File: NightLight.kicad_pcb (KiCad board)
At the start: 2 copper layers, 88 x 88 mm, 17 parts, among them U1 magnetic-charger, U2 rdm-6300, U3 TP4056, U4 ESP32-WROOM-32

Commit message: Add lots of ocmponents
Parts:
- added C1: 22u, Capacitor_THT:CP_Radial_D5.0mm_P2.50mm, F.Cu at (101.0, 116.2)
- added J1: Conn_01x02, Connector_PinHeader_2.54mm:PinHeader_1x02_P2.54mm_Vertical, F.Cu at (95.5, 93.5)
- added J2: Micro_SD_Card, sd-card:sd-card, F.Cu at (99.5, 121.2)
- added U5: AMS1117-3.3, Package_TO_SOT_SMD:SOT-223-3_TabPin2, B.Cu at (97.3, 111.3)
- D7, U1: moved to B.Cu
- moved U3 46.0 mm to (142.6, 109.8), turned to 180 degrees
- moved BT1 16.8 mm to (111.5, 108.8), turned to 180 degrees
- moved R1 16.7 mm to (89.5, 69.0), turned to 0 degrees
- moved D7 5.00 mm to (93.0, 65.0), turned to 180 degrees
- moved U4 5.00 mm to (73.0, 100.0)
- moved R2 2.25 mm to (111.2, 105.5)
- moved R3 2.25 mm to (111.2, 98.5)
- turned U1 to 180 degrees
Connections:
- U2 pad 6: unconnected-(U2-Pad6) -> Net-(J1-Pad1)
- U2 pad 7: unconnected-(U2-Pad7) -> Net-(J1-Pad2)
- U3 pad 3: +3V3 -> +4V
- U4 pad 10: unconnected-(U4-Pad10) -> DAC1
- U4 pad 11: unconnected-(U4-Pad11) -> DAC2
- U4 pad 12: unconnected-(U4-Pad12) -> TOUCH3
- U4 pad 8: unconnected-(U4-Pad8) -> TOUCH1
- U4 pad 9: unconnected-(U4-Pad9) -> TOUCH2
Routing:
- net Net-(D5-Pad1): track 70.8 -> 0.00 mm
- net unconnected-(U2-Pad4): track 42.7 -> 0.00 mm
- net PHOTO_VOLTAGE: track 38.8 -> 0.00 mm
- net GND: track 36.3 -> 0.00 mm
- net +5V: track 35.9 -> 0.00 mm
- net +3V3: track 35.1 -> 0.00 mm
- net Net-(D2-Pad1): track 35.0 -> 0.00 mm
- net +BATT: track 24.6 -> 0.00 mm
- net -BATT: track 13.1 -> 0.00 mm
- net ADC_BAT: track 1.92 -> 0.00 mm
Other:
- outline, holes or cut-outs redrawn
- board text added: "TODO: - Batterie ausmessen - Speaker Optionen auschecken - How far does the SD card protrude"

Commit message: Add button and update the magnetic charger
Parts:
- added R4: 10k, Resistor_THT:R_Axial_DIN0204_L3.6mm_D1.6mm_P5.08mm_Horizontal, F.Cu at (61.5, 82.8)
- added SW1: POWER-ON, Button_Switch_SMD:SW_SPDT_CK-JS102011SAQN, B.Cu at (128.6, 129.4)
- U5: footprint Package_TO_SOT_SMD:SOT-223-3_TabPin2 -> Package_TO_SOT_SMD:TO-252-2
- moved U5 4.15 mm to (93.3, 110.5)
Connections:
- U2 pad 4: unconnected-(U2-Pad4) -> RFID_TX
- U5 pad 3: +4V -> /+4V_Switched

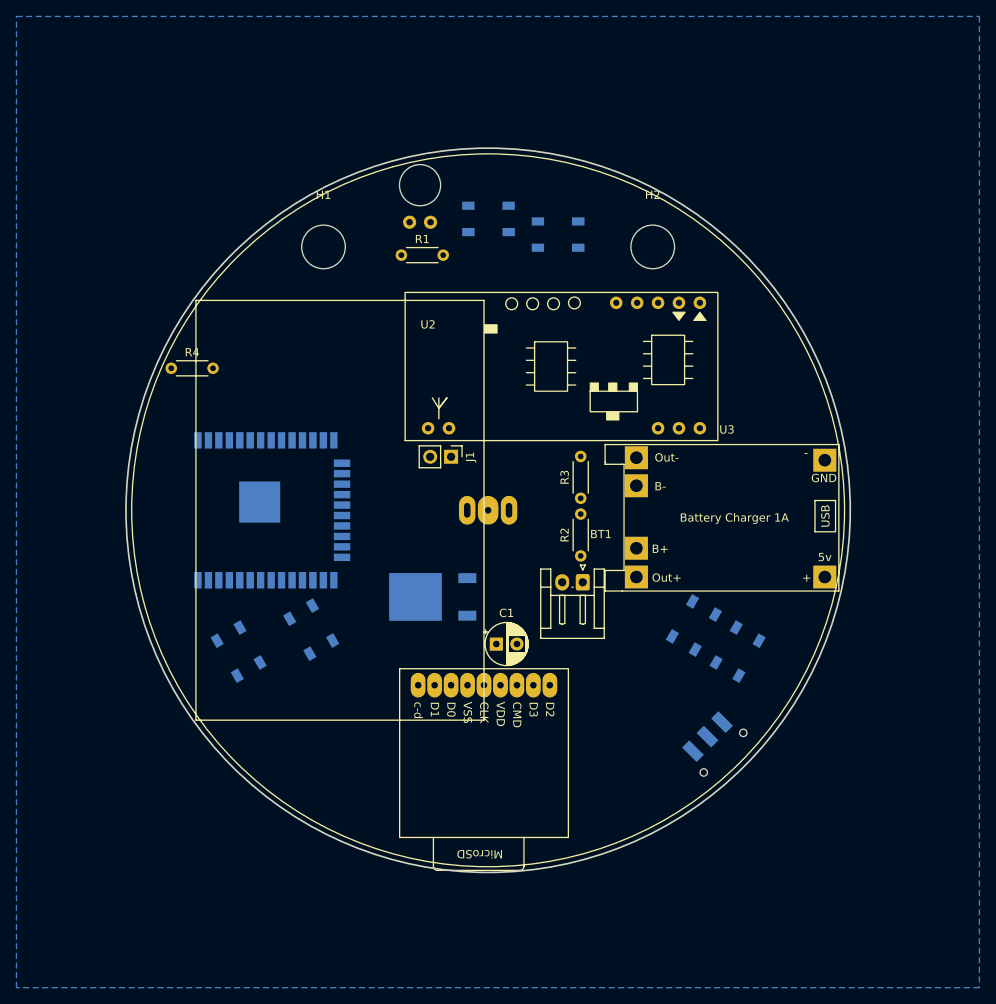
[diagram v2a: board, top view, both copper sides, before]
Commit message: Updates from card board prototype
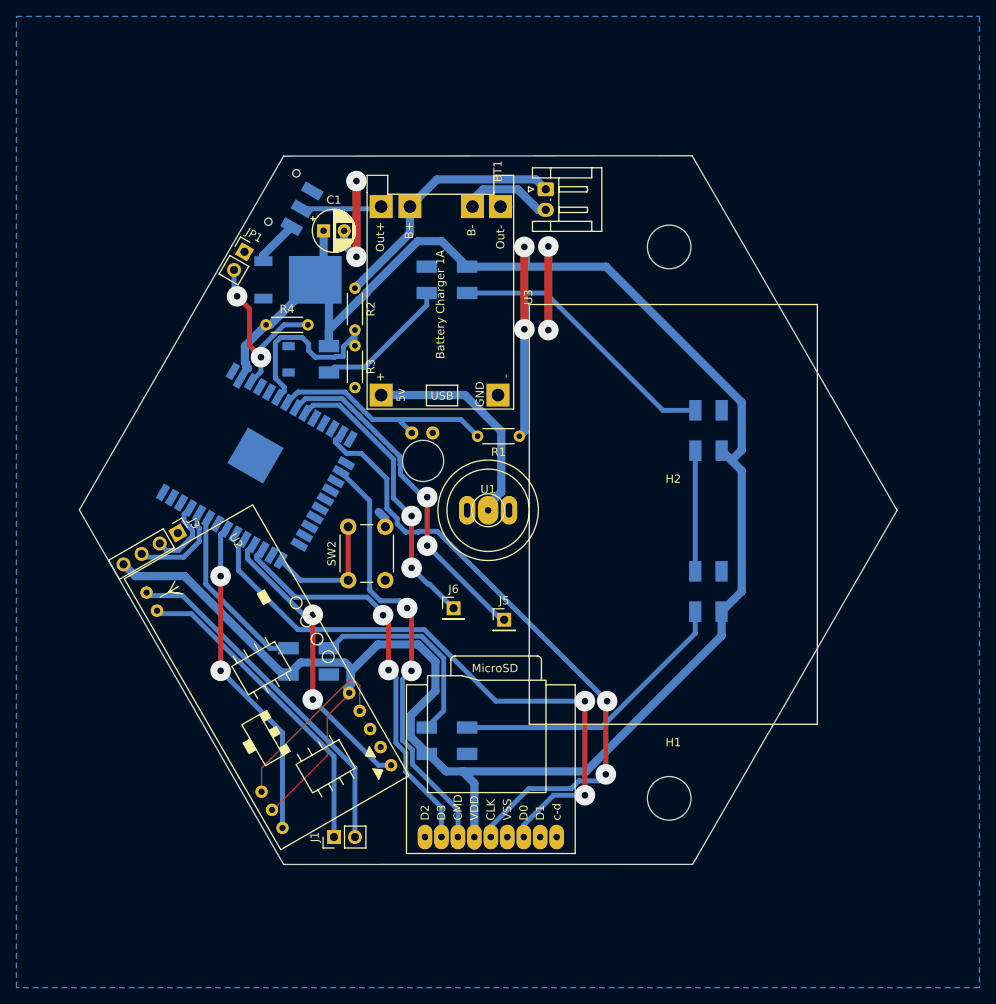
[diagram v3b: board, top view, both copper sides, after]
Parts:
- added J3: TTL, Connector_PinHeader_2.54mm:PinHeader_1x04_P2.54mm_Vertical, F.Cu at (62.3, 102.8)
- added J5: Touch1, Connector_PinHeader_2.54mm:PinHeader_1x01_P2.54mm_Vertical, F.Cu at (102.0, 113.3)
- added J6: Touch2, Connector_PinHeader_2.54mm:PinHeader_1x01_P2.54mm_Vertical, F.Cu at (95.8, 111.9)
- added JP1: Jumper_2_Open, Connector_PinHeader_2.54mm:PinHeader_1x02_P2.54mm_Vertical, F.Cu at (70.4, 68.6)
- added SW2: SW_Push, Button_Switch_THT:SW_PUSH_6mm_H4.3mm, F.Cu at (83.0, 108.5)
- U1: moved to F.Cu
- moved SW1 86.2 mm to (75.0, 62.0), turned to 60 degrees
- moved H1 78.9 mm to (122.5, 134.5)
- moved U2 63.5 mm to (79.0, 130.4), turned to -60 degrees
- moved U3 61.4 mm to (85.3, 87.7), turned to 90 degrees
- moved D1 60.1 mm to (78.2, 118.4), turned to 180 degrees
- moved C1 54.4 mm to (80.0, 66.0)
- moved D4 54.0 mm to (126.8, 90.3), turned to -90 degrees
- moved D5 51.8 mm to (95.0, 72.0), turned to 0 degrees
- moved J1 48.3 mm to (81.3, 139.7), turned to 90 degrees
- moved BT1 48.0 mm to (107.0, 61.0), turned to -90 degrees
- moved R2 42.6 mm to (83.8, 73.0), turned to -90 degrees
- moved U5 41.9 mm to (76.9, 72.0), turned to 0 degrees
- moved H2 34.6 mm to (122.5, 102.5)
- moved D2 33.1 mm to (95.0, 128.0), turned to 180 degrees
- moved R3 33.1 mm to (83.8, 80.0), turned to -90 degrees
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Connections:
- U4 pad 12: TOUCH3 -> unconnected-(U4-Pad12)
- U4 pad 28: unconnected-(U4-Pad28) -> RFID_TX
- U4 pad 31: unconnected-(U4-Pad31) -> RFID_LED
- U4 pad 33: unconnected-(U4-Pad33) -> Neopixel
- U4 pad 6: unconnected-(U4-Pad6) -> ADC_BAT
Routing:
- net +3V3: track 0.00 -> 288.6 mm, vias 0 -> 2
- net SCK: track 0.00 -> 77.8 mm, vias 0 -> 2
- net MISO: track 0.00 -> 74.5 mm, vias 0 -> 2
- net MOSI: track 0.00 -> 52.5 mm, vias 0 -> 2
- net CS: track 0.00 -> 49.6 mm, vias 0 -> 2
- net GND: track 0.00 -> 48.7 mm, vias 0 -> 4
- net Net-(J1-Pad2): track 0.00 -> 42.6 mm
- net TOUCH1: track 0.00 -> 41.5 mm, vias 0 -> 2
- net RFID_LED: track 0.00 -> 39.7 mm, vias 0 -> 2
- net Net-(J1-Pad1): track 0.00 -> 38.7 mm
- net RFID_TX: track 0.00 -> 35.9 mm, vias 0 -> 2
- net Net-(D2-Pad1): track 0.00 -> 35.1 mm
- net TOUCH2: track 0.00 -> 35.1 mm, vias 0 -> 2
- net Net-(D4-Pad1): track 0.00 -> 33.6 mm
- net +BATT: track 0.00 -> 31.0 mm
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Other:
- board size 88 x 88 mm -> 99.4 x 86.1 mm
- board text removed: "TODO: - Batterie ausmessen - Speaker Optionen auschecken - How far does the SD card protrude"

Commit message: Add version number
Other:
- board text added: "v0.1 - Januar 2023"
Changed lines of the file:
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@@
     ) (layer "Edge.Cuts") (width 0.1) (fill none))
   (gr_circle (center 92.1 94) (end 94.6 94) (layer "Edge.Cuts") (width 0.1) (fill none))
+  (gr_text "v0.1 - Januar 2023" (at 116 100.3 90) (layer "F.SilkS")
+    (effects (font (size 1.5 1.5) (thickness 0.3)))
+  )
   (segment (start 93.799501 59.800499) (end 90.5 63.1) (width 1) (layer "B.Cu") (net 1))
   (segment (start 83.82 73.01) (end 90.5 66.33) (width 1) (layer "B.Cu") (net 1))

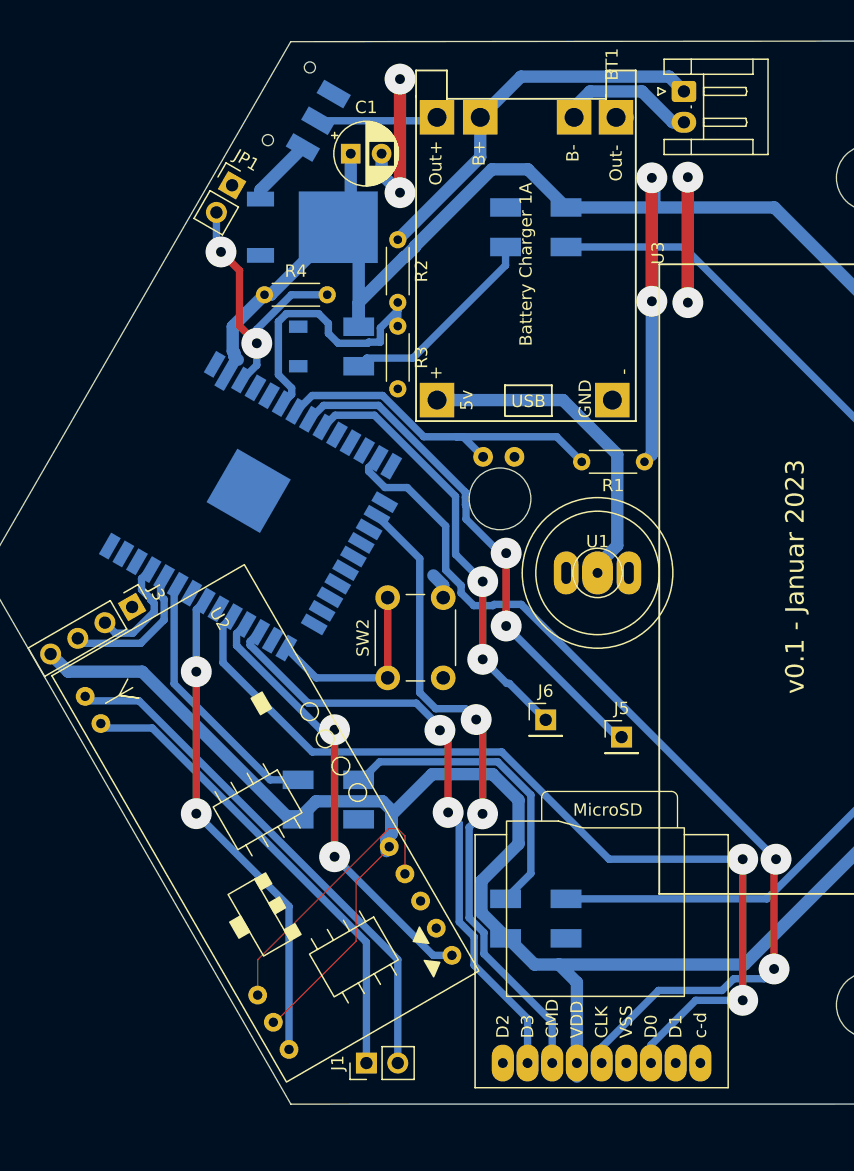
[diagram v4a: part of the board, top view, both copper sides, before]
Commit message: Add a speaker outlet
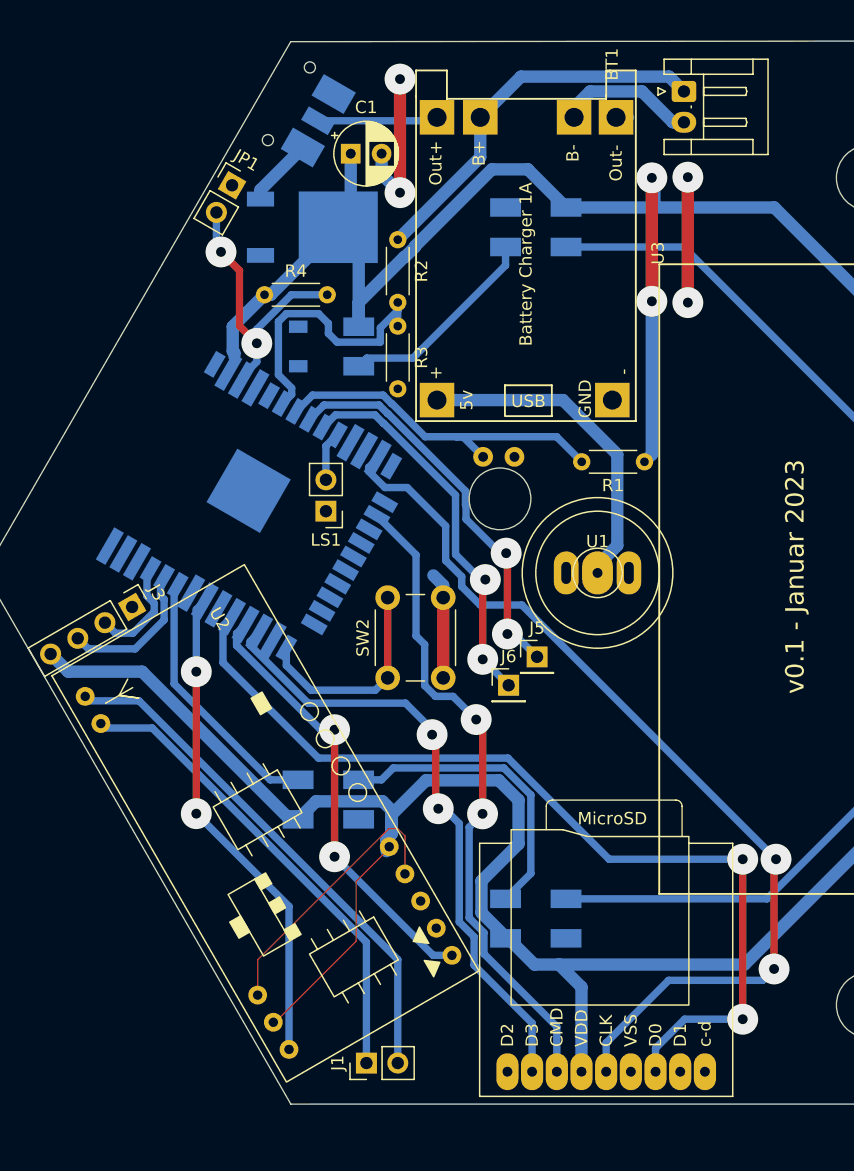
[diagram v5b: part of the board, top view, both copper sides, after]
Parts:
- added LS1: Speaker, Connector_PinHeader_2.54mm:PinHeader_1x02_P2.54mm_Vertical, F.Cu at (78.0, 95.0)
- moved J5 9.44 mm to (95.1, 106.8)
- moved J6 4.10 mm to (92.8, 109.1)
- moved J2 0.79 mm to (100.7, 140.4)
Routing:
- net TOUCH1: track 41.5 -> 32.4 mm
- net GND: track 48.7 -> 55.2 mm
- net DAC1: track 0.00 -> 4.01 mm
- net TOUCH2: track 35.1 -> 31.4 mm
- net BOOT: track 15.7 -> 17.4 mm
- net MISO: track 74.5 -> 75.6 mm
- net +3V3: track 288.6 -> 287.6 mm
- net SCK: track 77.8 -> 76.9 mm
- net CS: track 49.6 -> 50.2 mm
